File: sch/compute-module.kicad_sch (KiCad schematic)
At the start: 10 parts, among them J2 SAM10346-ND, J3 Conn_02x20_Odd_Even, M1 ComputeModule5-CM5, SW1 1825910-6

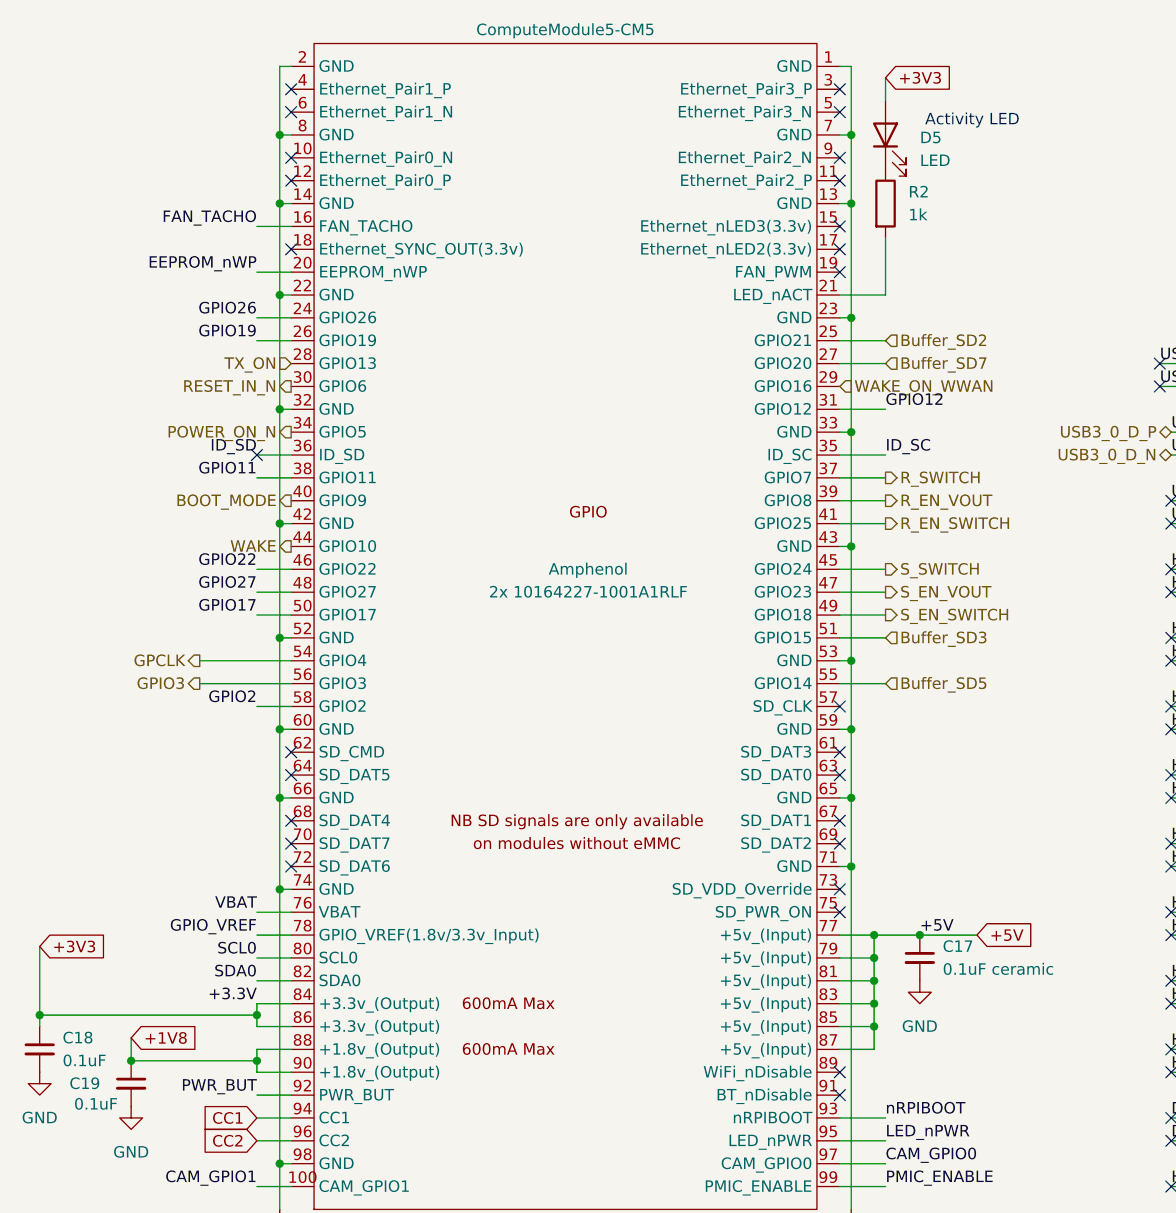
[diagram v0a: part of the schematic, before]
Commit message: added ports to powersupply
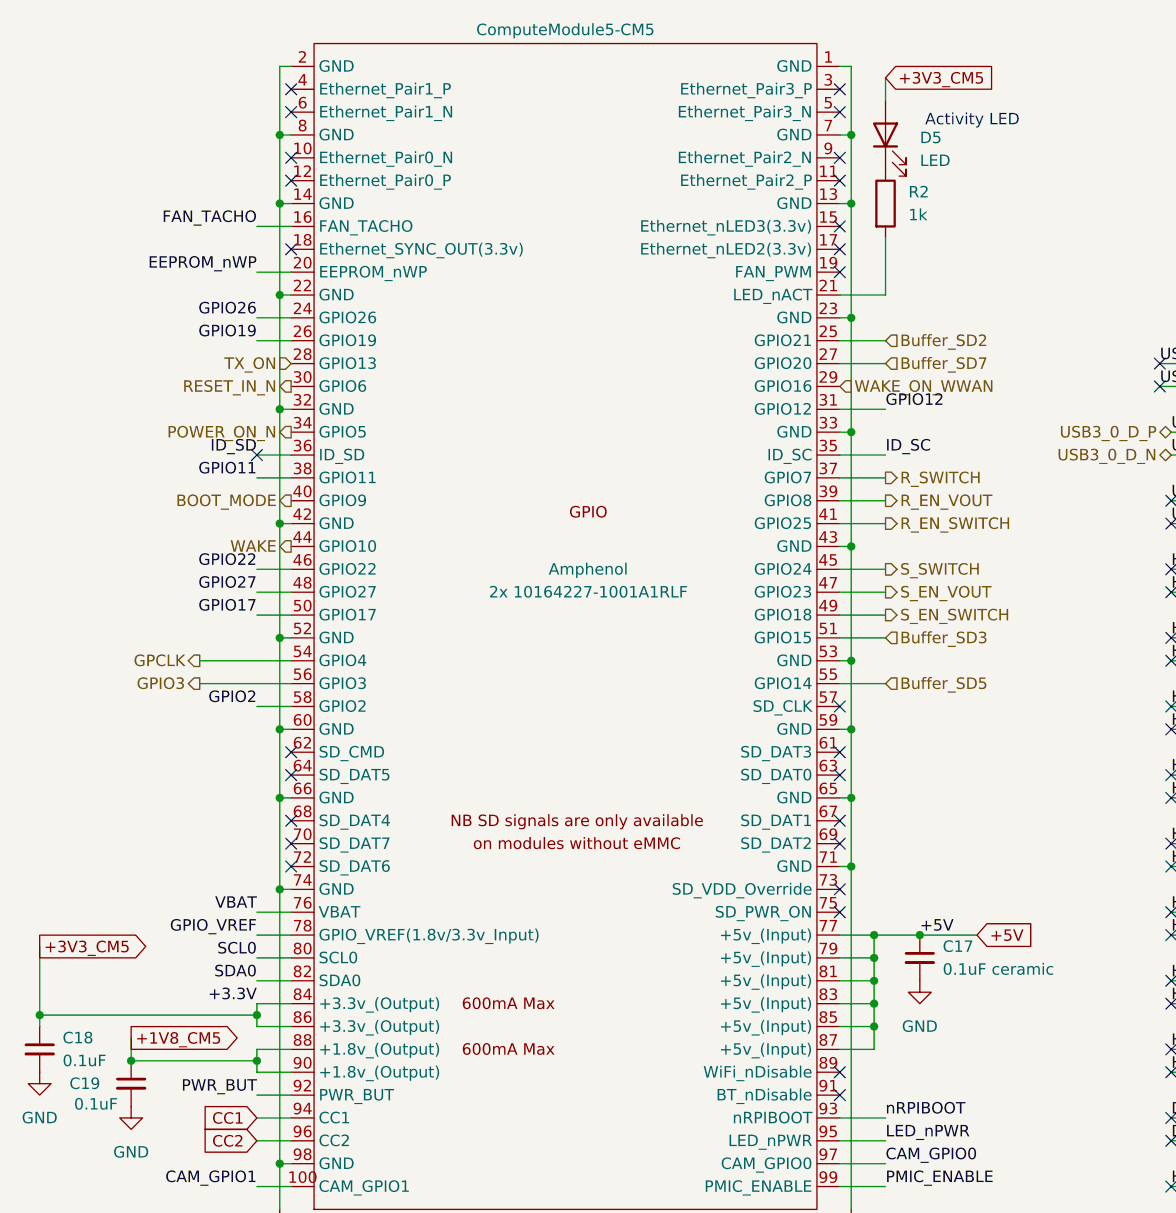
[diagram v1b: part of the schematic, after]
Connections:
- net +1V8 renamed +1V8_CM5
- net +3V3 renamed +3V3_CM5
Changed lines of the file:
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@@
 		)
 	)
-	(global_label "+3V3"
-		(shape input)
+	(global_label "+3V3_CM5"
+		(shape output)
 		(at 15.24 118.11 0)
 		(fields_autoplaced yes)
@@
 		)
 	)
-	(global_label "+3V3"
+	(global_label "+3V3_CM5"
 		(shape input)
 		(at 109.22 21.59 0)
@@
 		)
 	)
-	(global_label "+1V8"
-		(shape input)
+	(global_label "+1V8_CM5"
+		(shape output)
 		(at 25.4 128.27 0)
 		(fields_autoplaced yes)

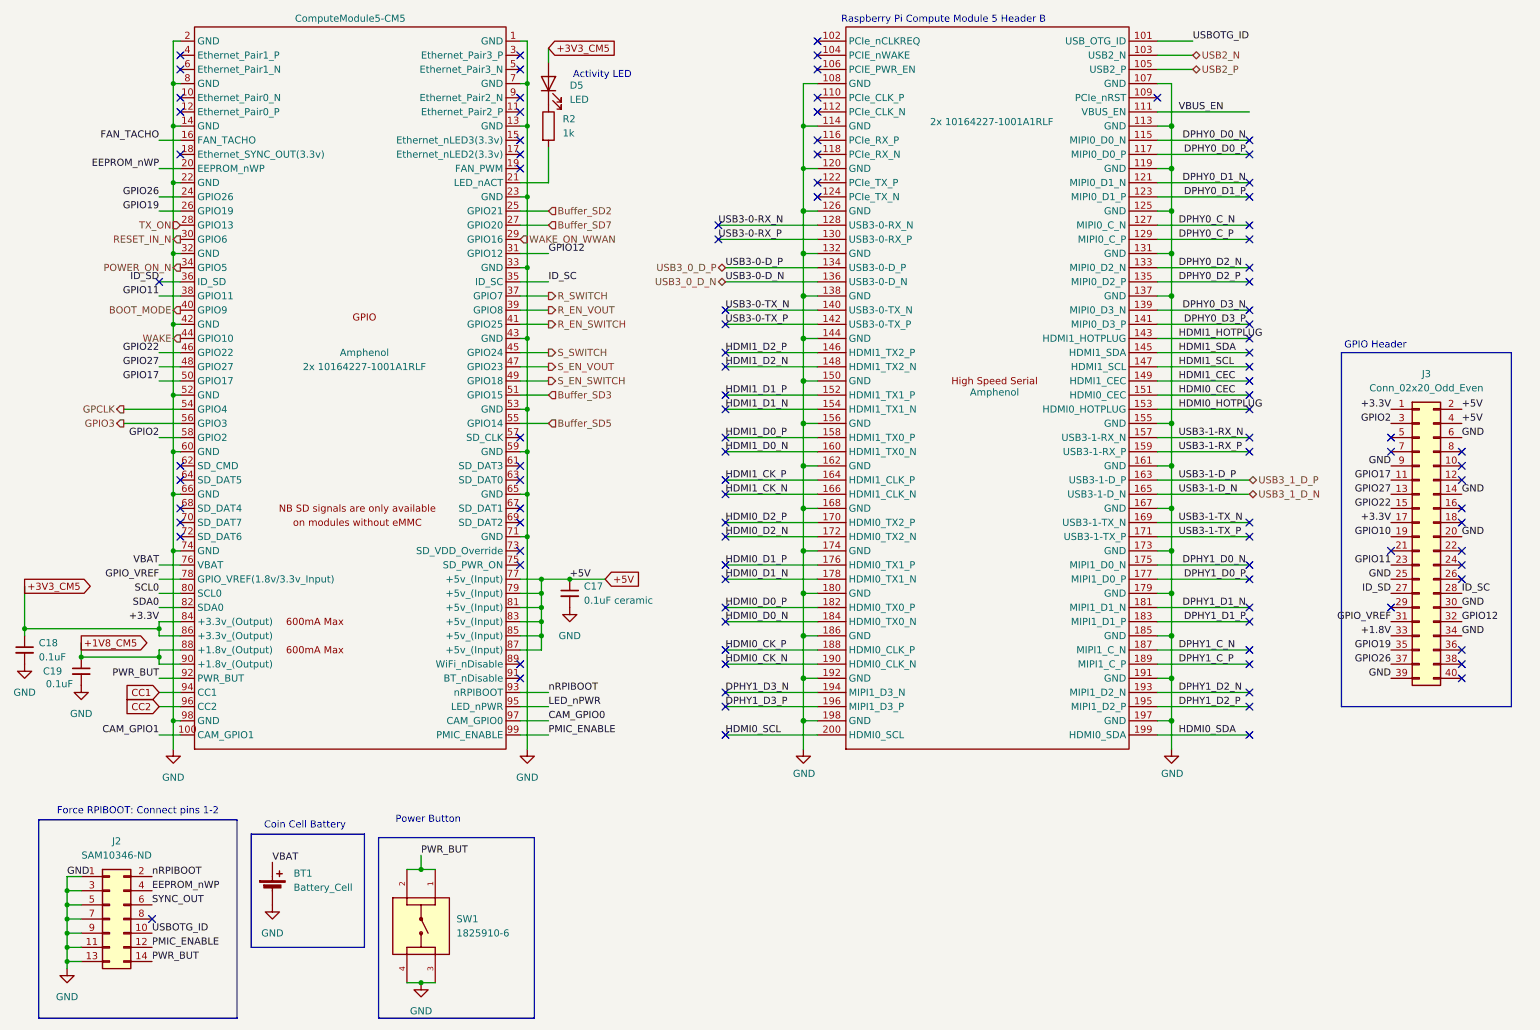
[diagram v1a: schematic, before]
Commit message: fix annotation and clean up schematics
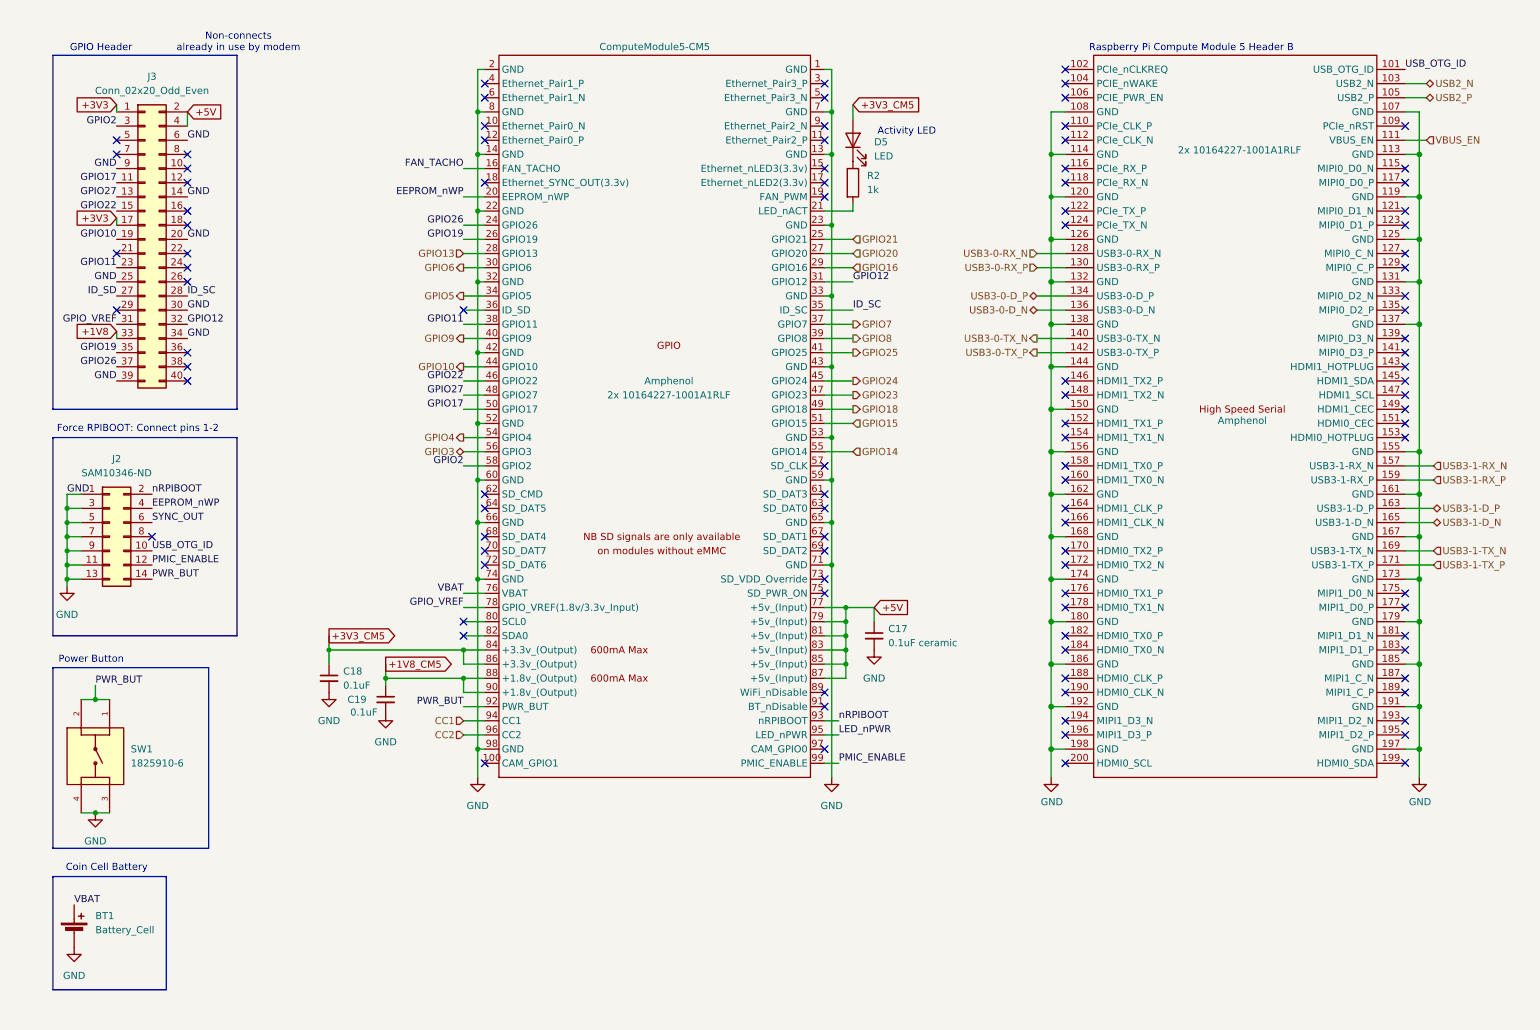
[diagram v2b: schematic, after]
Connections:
- net WAKE is gone; now on net GPIO10: M1.44 (GPIO10)
- net +3V3_CM5: no longer J3.1 (Pin_1), J3.17 (Pin_17)
- net ID_SD: no longer M1.36 (ID_SD)
- net +1.8V renamed +1V8
- net BOOT_MODE renamed GPIO9
- net Buffer_SD2 renamed GPIO21
- net Buffer_SD3 renamed GPIO15
- net Buffer_SD5 renamed GPIO14
- net Buffer_SD7 renamed GPIO20
- net CAM_GPIO0: no longer names the net of M1.97 (CAM_GPIO0)
- net CAM_GPIO1: no longer names the net of M1.100 (CAM_GPIO1)
- net DPHY0_C_N: no longer names the net of M1.127 (MIPI0_C_N)
- net DPHY0_C_P: no longer names the net of M1.129 (MIPI0_C_P)
- net DPHY0_D0_N: no longer names the net of M1.115 (MIPI0_D0_N)
- net DPHY0_D0_P: no longer names the net of M1.117 (MIPI0_D0_P)
- net DPHY0_D1_N: no longer names the net of M1.121 (MIPI0_D1_N)
- net DPHY0_D1_P: no longer names the net of M1.123 (MIPI0_D1_P)
- net DPHY0_D2_N: no longer names the net of M1.133 (MIPI0_D2_N)
- net DPHY0_D2_P: no longer names the net of M1.135 (MIPI0_D2_P)
- net DPHY0_D3_N: no longer names the net of M1.139 (MIPI0_D3_N)
- net DPHY0_D3_P: no longer names the net of M1.141 (MIPI0_D3_P)
- net DPHY1_C_N: no longer names the net of M1.187 (MIPI1_C_N)
- net DPHY1_C_P: no longer names the net of M1.189 (MIPI1_C_P)
- net DPHY1_D0_N: no longer names the net of M1.175 (MIPI1_D0_N)
- net DPHY1_D0_P: no longer names the net of M1.177 (MIPI1_D0_P)
- net DPHY1_D1_N: no longer names the net of M1.181 (MIPI1_D1_N)
- net DPHY1_D1_P: no longer names the net of M1.183 (MIPI1_D1_P)
- net DPHY1_D2_N: no longer names the net of M1.193 (MIPI1_D2_N)
- net DPHY1_D2_P: no longer names the net of M1.195 (MIPI1_D2_P)
- net DPHY1_D3_N: no longer names the net of M1.194 (MIPI1_D3_N)
- net DPHY1_D3_P: no longer names the net of M1.196 (MIPI1_D3_P)
- net GPCLK renamed GPIO4
- net HDMI0_CEC: no longer names the net of M1.151 (HDMI0_CEC)
- net HDMI0_CK_N: no longer names the net of M1.190 (HDMI0_CLK_N)
- net HDMI0_CK_P: no longer names the net of M1.188 (HDMI0_CLK_P)
- net HDMI0_D0_N: no longer names the net of M1.184 (HDMI0_TX0_N)
- net HDMI0_D0_P: no longer names the net of M1.182 (HDMI0_TX0_P)
- net HDMI0_D1_N: no longer names the net of M1.178 (HDMI0_TX1_N)
- net HDMI0_D1_P: no longer names the net of M1.176 (HDMI0_TX1_P)
- net HDMI0_D2_N: no longer names the net of M1.172 (HDMI0_TX2_N)
- net HDMI0_D2_P: no longer names the net of M1.170 (HDMI0_TX2_P)
- net HDMI0_HOTPLUG: no longer names the net of M1.153 (HDMI0_HOTPLUG)
- net HDMI0_SCL: no longer names the net of M1.200 (HDMI0_SCL)
- net HDMI0_SDA: no longer names the net of M1.199 (HDMI0_SDA)
- net HDMI1_CEC: no longer names the net of M1.149 (HDMI1_CEC)
- net HDMI1_CK_N: no longer names the net of M1.166 (HDMI1_CLK_N)
- net HDMI1_CK_P: no longer names the net of M1.164 (HDMI1_CLK_P)
- net HDMI1_D0_N: no longer names the net of M1.160 (HDMI1_TX0_N)
- net HDMI1_D0_P: no longer names the net of M1.158 (HDMI1_TX0_P)
- net HDMI1_D1_N: no longer names the net of M1.154 (HDMI1_TX1_N)
- net HDMI1_D1_P: no longer names the net of M1.152 (HDMI1_TX1_P)
- net HDMI1_D2_N: no longer names the net of M1.148 (HDMI1_TX2_N)
- net HDMI1_D2_P: no longer names the net of M1.146 (HDMI1_TX2_P)
- net HDMI1_HOTPLUG: no longer names the net of M1.143 (HDMI1_HOTPLUG)
- net HDMI1_SCL: no longer names the net of M1.147 (HDMI1_SCL)
- net HDMI1_SDA: no longer names the net of M1.145 (HDMI1_SDA)
- net POWER_ON_N renamed GPIO5
- net RESET_IN_N renamed GPIO6
- net R_EN_SWITCH renamed GPIO25
- net R_EN_VOUT renamed GPIO8
- net R_SWITCH renamed GPIO7
- net SCL0: no longer names the net of M1.80 (SCL0)
- net SDA0: no longer names the net of M1.82 (SDA0)
- net S_EN_SWITCH renamed GPIO18
- net S_EN_VOUT renamed GPIO23
- net S_SWITCH renamed GPIO24
- net TX_ON renamed GPIO13
- net USB3_0_D_N renamed USB3-0-D_N
- net USB3_0_D_P renamed USB3-0-D_P
- net USB3_1_D_N renamed USB3-1-D_N
- net USB3_1_D_P renamed USB3-1-D_P
- net USBOTG_ID renamed USB_OTG_ID
- net WAKE_ON_WWAN renamed GPIO16
- new net +3V3: J3.1 (Pin_1), J3.17 (Pin_17)
- no-connect marks 105 -> 101
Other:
- note added: "Non-connects already in use by modem"
- moved on the sheet: BT1, C17, C18, C19, D5, J2, J3, R2, SW1

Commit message: work pcb about 70 percent
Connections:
- net GPIO_VREF is gone; now on net +3V3_CM5: J3.31 (Pin_31), M1.78 (GPIO_VREF(1.8v/3.3v_Input))
- net GPIO10: no longer J3.19 (Pin_19)
- no-connect marks 101 -> 102
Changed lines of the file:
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@@
+	)
+	(junction
+		(at 86.36 129.54)
+		(diameter 0)
+		(color 0 0 0 0)
 	)
 	(junction
@@
 	)
 	(no_connect
+		(at 31.75 55.88)
+	)
+	(no_connect
 		(at 262.89 60.96)
 	)
@@
 	(wire
 		(pts
+			(xy 86.36 129.54) (xy 86.36 121.92)
+		)
+		(stroke
+			(width 0)
+			(type default)
+		)
+	)
+	(wire
+		(pts
 			(xy 199.39 55.88) (xy 201.93 55.88)
 		)
@@
 	(wire
 		(pts
+			(xy 86.36 121.92) (xy 97.79 121.92)
+		)
+		(stroke
+			(width 0)
+			(type default)
+		)
+	)
+	(wire
+		(pts
 			(xy 158.75 93.98) (xy 163.83 93.98)
 		)
@@
 	(wire
 		(pts
-			(xy 93.98 121.92) (xy 97.79 121.92)
-		)
-		(stroke
-			(width 0)
-			(type default)
-		)
-	)
-	(wire
-		(pts
 			(xy 199.39 78.74) (xy 199.39 86.36)
 		)
@@
 	(wire
 		(pts
+			(xy 86.36 129.54) (xy 93.98 129.54)
+		)
+		(stroke
+			(width 0)
+			(type default)
+		)
+	)
+	(wire
+		(pts
 			(xy 31.75 52.07) (xy 31.75 53.34)
 		)
@@
 	(wire
 		(pts
-			(xy 69.85 129.54) (xy 93.98 129.54)
+			(xy 69.85 129.54) (xy 86.36 129.54)
 		)
 		(stroke
@@
 		(effects
 			(font
-				(size 1.27 1.27)
-			)
-			(justify right bottom)
-		)
-	)
-	(label "GPIO10"
-		(at 31.75 55.88 180)
-		(effects
-			(font
